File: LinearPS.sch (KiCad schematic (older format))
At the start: 84 parts, among them J1 Conn_01x03, J2 Conn_01x02, J3 Conn_01x03, J4 Conn_01x01, J5 Conn_01x01, J6 Conn_01x01, J7 Conn_01x01, J8 Conn_01x02, Q1 2N2222, Q2 TIP41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

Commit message: Added outputs for voltage and current meters
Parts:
- removed R28, R29: 10k, Resistors_THT:R_Axial_DIN0207_L6.3mm_D2.5mm_P7.62mm_Horizontal, symbol R
- removed U3: LM7805_TO220, TO_SOT_Packages_THT:TO-220-3_Vertical, symbol LM7805_TO220
- added D22: 1N4733A, Diodes_THT:D_DO-41_SOD81_P7.62mm_Horizontal, symbol D_Zener
- added J9: Conn_01x02, Pin_Headers:Pin_Header_Straight_1x02_Pitch2.54mm, symbol Conn_01x02
- added R32: 1k, Resistors_THT:R_Axial_DIN0411_L9.9mm_D3.6mm_P12.70mm_Horizontal, symbol R
- added RV3, RV4, RV5: 10k, Potentiometers:Potentiometer_Trimmer_Bourns_3296W, symbol POT
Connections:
- wire segments 174 -> 184
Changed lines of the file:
@@
-$EndComp
-$Comp
-L R R29
-U 1 1 5CECC88D
-P 10500 5750
-F 0 "R29" V 10580 5750 50  0000 C CNN
-F 1 "10k" V 10500 5750 50  0000 C CNN
-F 2 "Resistors_THT:R_Axial_DIN0207_L6.3mm_D2.5mm_P7.62mm_Horizontal" V 10430 5750 50  0001 C CNN
-F 3 "" H 10500 5750 50  0001 C CNN
-	1    10500 5750
-	0    1    1    0
-$EndComp
-$Comp
-L R R28
-U 1 1 5CECD45F
-P 10150 5650
-F 0 "R28" V 10230 5650 50  0000 C CNN
-F 1 "10k" V 10150 5650 50  0000 C CNN
-F 2 "Resistors_THT:R_Axial_DIN0207_L6.3mm_D2.5mm_P7.62mm_Horizontal" V 10080 5650 50  0001 C CNN
-F 3 "" H 10150 5650 50  0001 C CNN
-	1    10150 5650
-	0    1    1    0
 $EndComp
 $Comp
@@
 $EndComp
 $Comp
-L LM7805_TO220 U3
-U 1 1 5CECF306
-P 2750 2100
-F 0 "U3" H 2600 2225 50  0000 C CNN
-F 1 "LM7805_TO220" H 2750 2225 50  0000 L CNN
-F 2 "TO_SOT_Packages_THT:TO-220-3_Vertical" H 2750 2325 50  0001 C CIN
-F 3 "" H 2750 2050 50  0001 C CNN
-	1    2750 2100
-	1    0    0    -1
-$EndComp
-$Comp
 L GND #PWR2
 U 1 1 5CECFA19
-P 2750 2450
-F 0 "#PWR2" H 2750 2200 50  0001 C CNN
-F 1 "GND" H 2750 2300 50  0000 C CNN
-F 2 "" H 2750 2450 50  0001 C CNN
-F 3 "" H 2750 2450 50  0001 C CNN
-	1    2750 2450
+P 2900 2450
+F 0 "#PWR2" H 2900 2200 50  0001 C CNN
+F 1 "GND" H 2900 2300 50  0000 C CNN
+F 2 "" H 2900 2450 50  0001 C CNN
+F 3 "" H 2900 2450 50  0001 C CNN
+	1    2900 2450
 	1    0    0    -1
 $EndComp
@@
 Connection ~ 5950 3200
 Wire Wire Line
-	5700 3200 5950 3200
+	5700 3200 6050 3200
 Wire Wire Line
 	5950 3000 5050 3000
@@
 	10950 5000 10850 5000
 Wire Wire Line
-	10650 5750 10900 5750
+	10500 5750 10900 5750
 Connection ~ 10950 5000
 Wire Wire Line
@@
 	10850 5300 10850 5000
 Wire Wire Line
-	10300 5650 10900 5650
-Wire Wire Line
-	10000 5700 10000 5650
+	10150 5650 10900 5650
 Wire Wire Line
 	2550 3950 2550 4200
@@
 Connection ~ 2550 3050
 Wire Wire Line
-	2750 2400 2750 2450
-Wire Wire Line
 	3450 2450 3450 2200
 Wire Wire Line
 	3450 2200 3600 2200
 Wire Wire Line
-	3050 2100 3600 2100
+	2800 2100 3600 2100
 Wire Wire Line
 	3150 2450 3150 2450
 Wire Wire Line
-	2300 2100 2450 2100
+	2300 2100 2500 2100
 Wire Wire Line
 	3150 2100 3150 2150
@@
 Wire Wire Line
 	1800 4050 1800 4200
+$Comp
+L R R32
+U 1 1 5CEDBDE6
+P 2650 2100
+F 0 "R32" V 2730 2100 50  0000 C CNN
+F 1 "1k" V 2650 2100 50  0000 C CNN
+F 2 "Resistors_THT:R_Axial_DIN0411_L9.9mm_D3.6mm_P12.70mm_Horizontal" V 2580 2100 50  0001 C CNN
+F 3 "" H 2650 2100 50  0001 C CNN
+	1    2650 2100
+	0    1    1    0
+$EndComp
+$Comp
+L D_Zener D22
+U 1 1 5CEDC7D4
+P 2900 2250
+F 0 "D22" H 2900 2350 50  0000 C CNN
+F 1 "1N4733A" H 2900 2150 50  0000 C CNN
+F 2 "Diodes_THT:D_DO-41_SOD81_P7.62mm_Horizontal" H 2900 2250 50  0001 C CNN
+F 3 "" H 2900 2250 50  0001 C CNN
+	1    2900 2250
+	0    1    1    0
+$EndComp
+Connection ~ 2900 2100
+Wire Wire Line
+	2900 2450 2900 2400
+$Comp
+L POT RV4
+U 1 1 5CEDA0AA
+P 10000 5900
+F 0 "RV4" V 9825 5900 50  0000 C CNN
+F 1 "10k" V 9900 5900 50  0000 C CNN
+F 2 "Potentiometers:Potentiometer_Trimmer_Bourns_3296W" H 10000 5900 50  0001 C CNN
+F 3 "" H 10000 5900 50  0001 C CNN
+	1    10000 5900
+	1    0    0    -1
+$EndComp
+Wire Wire Line
+	10200 5550 10200 6050
+Wire Wire Line
+	10200 6050 10000 6050
+Connection ~ 10200 5550
+Wire Wire Line
+	10150 5900 10150 5650
+Wire Wire Line
+	10000 5700 10000 5750
+$Comp
+L POT RV5
+U 1 1 5CEDAE92
+P 10350 5900
+F 0 "RV5" V 10175 5900 50  0000 C CNN
+F 1 "10k" V 10250 5900 50  0000 C CNN
+F 2 "Potentiometers:Potentiometer_Trimmer_Bourns_3296W" H 10350 5900 50  0001 C CNN
+F 3 "" H 10350 5900 50  0001 C CNN
+	1    10350 5900
+	1    0    0    -1
+$EndComp
+Wire Wire Line
+	10500 5900 10500 5750
+Wire Wire Line
+	10650 5550 10650 6050
+Wire Wire Line
+	10650 6050 10350 6050
+Connection ~ 10650 5550
+$Comp
+L POT RV3
+U 1 1 5CEDB3D7
+P 5600 4500
+F 0 "RV3" V 5425 4500 50  0000 C CNN
+F 1 "10k" V 5500 4500 50  0000 C CNN
+F 2 "Potentiometers:Potentiometer_Trimmer_Bourns_3296W" H 5600 4500 50  0001 C CNN
+F 3 "" H 5600 4500 50  0001 C CNN
+	1    5600 4500
+	-1   0    0    1
+$EndComp
+Wire Wire Line
+	5600 4650 5600 4800
+Connection ~ 5600 4800
+Wire Wire Line
+	5450 4500 5400 4500
+Wire Wire Line
+	5400 4500 5400 4200
+Connection ~ 5400 4200
+$Comp
+L Conn_01x02 J9
+U 1 1 5CEDB976
+P 6250 3200
+F 0 "J9" H 6250 3300 50  0000 C CNN
+F 1 "Conn_01x02" H 6250 3000 50  0000 C CNN
+F 2 "Pin_Headers:Pin_Header_Straight_1x02_Pitch2.54mm" H 6250 3200 50  0001 C CNN
+F 3 "" H 6250 3200 50  0001 C CNN
+	1    6250 3200
+	1    0    0    -1
+$EndComp
+Wire Wire Line
+	6050 3300 6050 4800
+Connection ~ 6050 4800
 $EndSCHEMATC

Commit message: Added better TO-220 mounting
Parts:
- removed D10: 1N4148, Diodes_THT:D_DO-35_SOD27_P7.62mm_Horizontal, symbol D
- removed D7: 1N5339B, Diodes_THT:D_DO-41_SOD81_P7.62mm_Horizontal, symbol D_Zener
- removed J9: Conn_01x02, Pin_Headers:Pin_Header_Straight_1x02_Pitch2.54mm, symbol Conn_01x02
- removed R15: 1k, Resistors_THT:R_Axial_DIN0411_L9.9mm_D3.6mm_P12.70mm_Horizontal, symbol R
- added C13: 100 nF, Capacitors_THT:C_Disc_D5.0mm_W2.5mm_P5.00mm, symbol C
- added D10: 1N4740A, Diodes_THT:D_DO-41_SOD81_P7.62mm_Horizontal, symbol D_Zener
- added D23, D7: 1N4148, Diodes_THT:D_DO-35_SOD27_P7.62mm_Horizontal, symbol D
- added JP1: Jumper_NO_Small, Pin_Headers:Pin_Header_Straight_1x02_Pitch2.54mm, symbol Jumper_NO_Small
- added RV6: 20k, Potentiometers:Potentiometer_Trimmer_Bourns_3296W, symbol POT
- Q2, Q4, Q5, Q6, Q7: footprint TO_SOT_Packages_THT:TO-220-3_Vertical -> linearps:TO-220-3_Vertical_WithPads
- R13: value 56k -> 22k
- R14: value 1k5 -> 1k
- R18: value 56k -> 33k
- RV3: value 10k -> 100k
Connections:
- net GND: now also U2.4 (V-), C13.1, D7.2 (A), JP1.1
- net at C1.1, C10.1, C11.1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: now also D10.1 (K); no longer Q3.1 (E), R19.1, U1.8 (V+)
- net at C4.1, C5.1, C7.2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: now also RV6.1; no longer R11.1, RV3.1
- net at R14.1, R3.1, U1.4 (V-): now also D23.1 (K), JP1.2; no longer U2.4 (V-)
- net at D8.1 (K), R5.2, RV1.1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: now also RV3.2; no longer R18.1
- net at R5.1, R6.1, U1.5 (+): no longer RV3.2
- net at C9.1, Q1.3 (C), U2.1: now also Q2.1 (B)
- net at RV3.3: now also R18.1
- new net: C13.2, D10.2 (A), Q3.1 (E), R19.1, U1.8 (V+)
- new net: R11.1, RV6.2
- new net: D23.2 (A), D7.1 (K)
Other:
- moved on the sheet: C9, R11

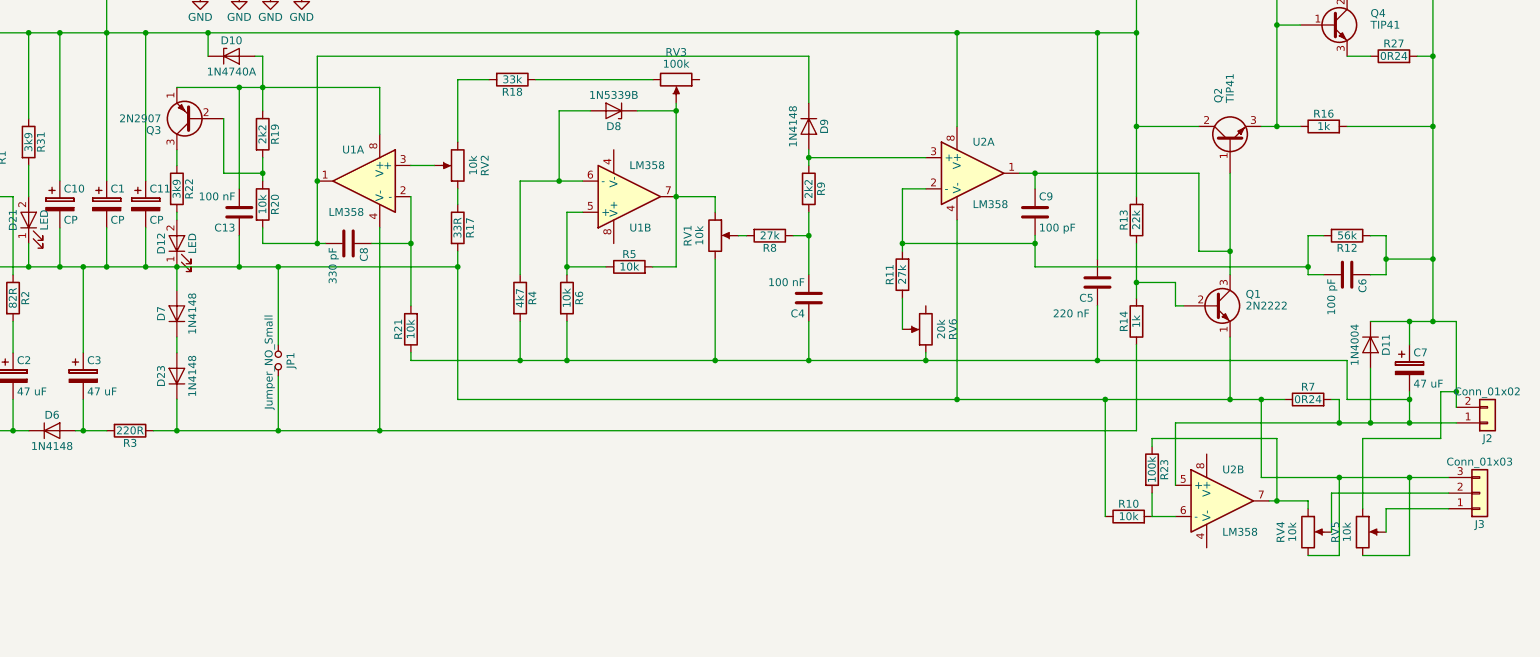
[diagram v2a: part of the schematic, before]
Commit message: Change the voltage and current sense output
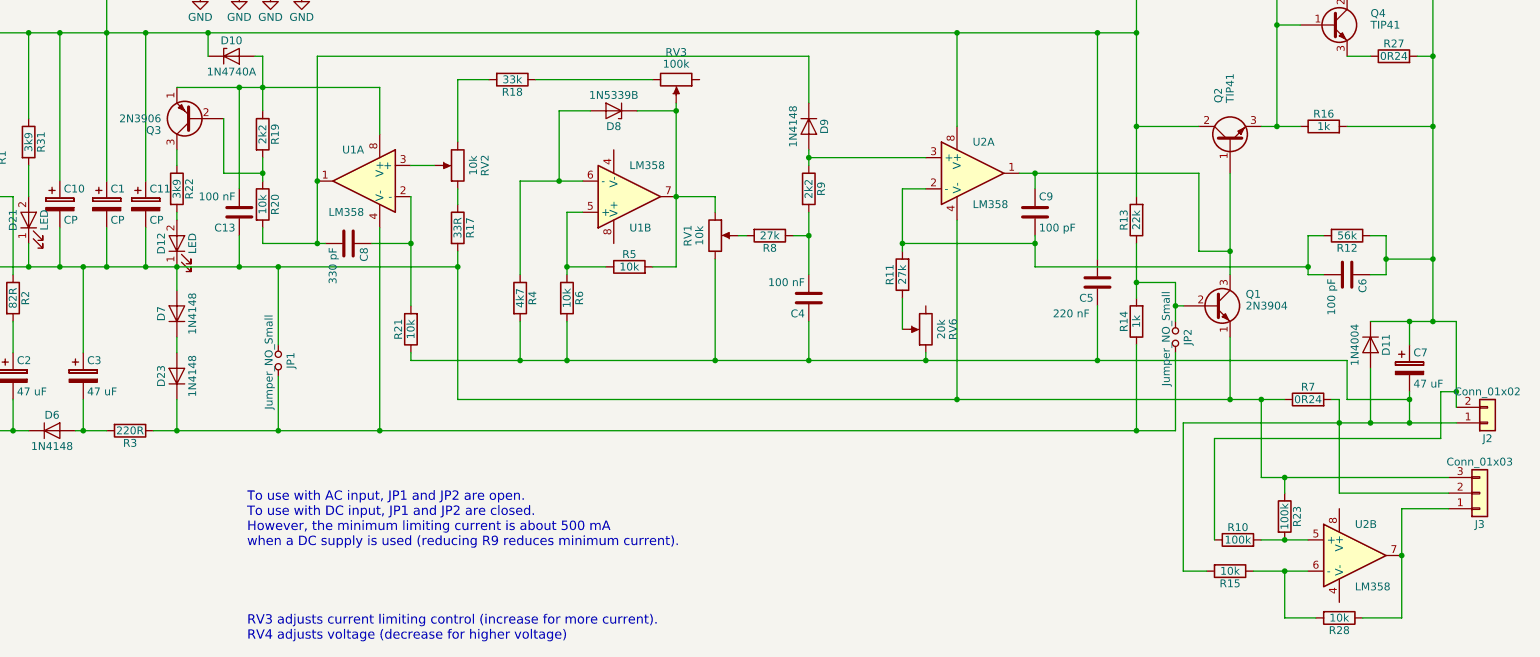
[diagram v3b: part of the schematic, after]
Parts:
- removed RV4, RV5: 10k, Potentiometers:Potentiometer_Trimmer_Bourns_3296W, symbol POT
- added JP2: Jumper_NO_Small, Pin_Headers:Pin_Header_Straight_1x02_Pitch2.54mm, symbol Jumper_NO_Small
- added R15, R28: 10k, Resistors_THT:R_Axial_DIN0207_L6.3mm_D2.5mm_P7.62mm_Horizontal, symbol R
- Q1: value 2N2222 -> 2N3904
- Q3: value 2N2907 -> 2N3906
- R10: value 10k -> 100k
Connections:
- net GND: now also R23.1; no longer R10.1
- net at C4.1, C5.1, C7.2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: now also J3.2 (Pin_2), R15.2; no longer U2.5 (+)
- net at C6.1, C7.1, D11.1 (K)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: now also R10.1
- net at D23.1 (K), JP1.2, R14.1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: now also JP2.2
- net at R10.2, R23.2: now also U2.5 (+); no longer U2.6 (-)
- net at U2.7: now also J3.1 (Pin_1), R28.1; no longer R23.1
- net at Q1.2 (B), R13.1, R14.2: now also JP2.1
- new net: R15.1, R28.2, U2.6 (-)
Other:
- note added: "RV3 adjusts current limiting control (increase for more current).\nRV4 adjusts voltage (decrease for higher voltage)"
- note added: "To use with AC input, JP1 and JP2 are open.\nTo use with DC input, JP1 and JP2 are closed. \nHowever, the minimum limiting current is about 500 mA\nwhen a DC supply is used (reducing R9 reduces minimum current)."
- moved on the sheet: R10, R23, U2B

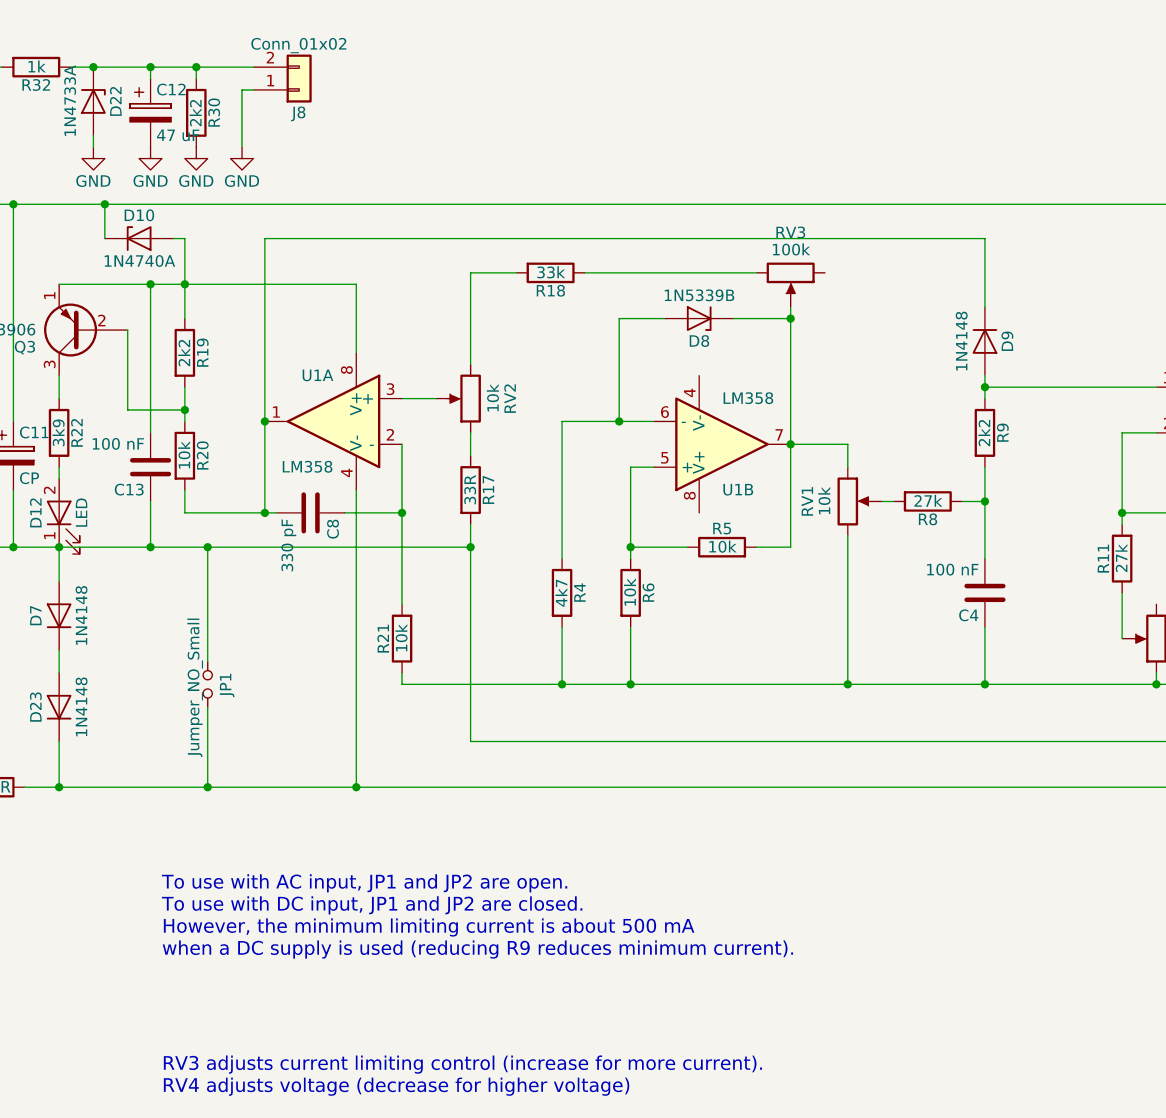
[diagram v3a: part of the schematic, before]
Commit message: Changed voltage and current meter output
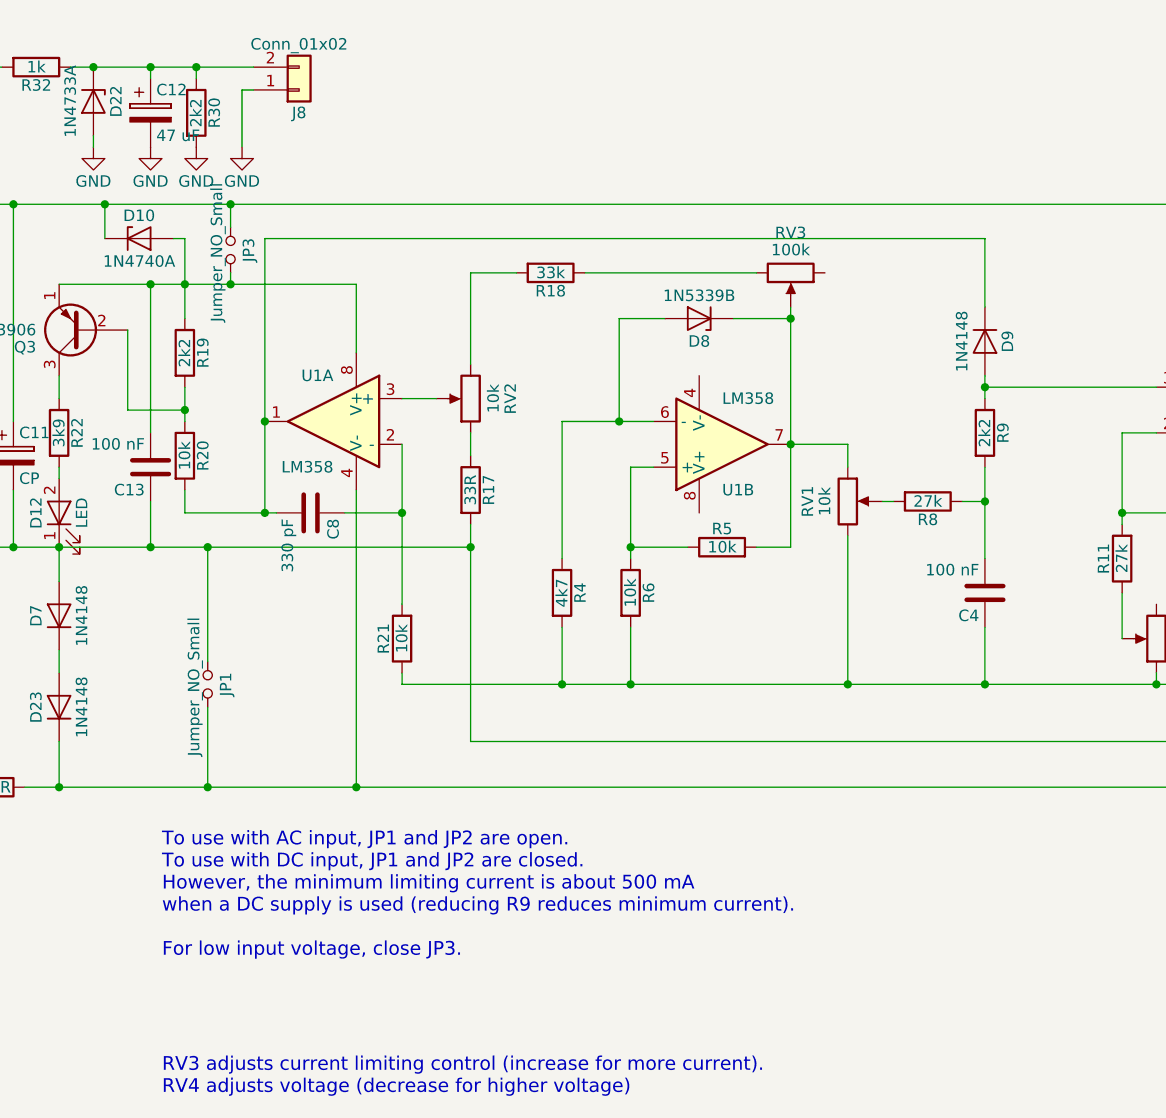
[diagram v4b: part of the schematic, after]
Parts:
- added JP3: Jumper_NO_Small, Pin_Headers:Pin_Header_Straight_1x02_Pitch2.54mm, symbol Jumper_NO_Small
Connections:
- net at C1.1, C10.1, C11.1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: now also JP3.1
- net at C13.2, D10.2 (A), Q3.1 (E)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: now also JP3.2
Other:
- note added: "To use with AC input, JP1 and JP2 are open.\nTo use with DC input, JP1 and JP2 are closed. \nHowever, the minimum limiting current is about 500 mA\nwhen a DC supply is used (reducing R9 reduces minimum current).\n\nFor low input voltage, close JP3."
- note removed: "To use with AC input, JP1 and JP2 are open.\nTo use with DC input, JP1 and JP2 are closed. \nHowever, the minimum limiting current is about 500 mA\nwhen a DC supply is used (reducing R9 reduces minimum current)."
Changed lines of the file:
@@
 $EndComp
 $Comp
-L GND #PWR01
+L GND #PWR1
 U 1 1 5CEC838A
 P 950 4450
-F 0 "#PWR01" H 950 4200 50  0001 C CNN
+F 0 "#PWR1" H 950 4200 50  0001 C CNN
 F 1 "GND" H 950 4300 50  0000 C CNN
 F 2 "" H 950 4450 50  0001 C CNN
@@
 $EndComp
 $Comp
-L GND #PWR02
+L GND #PWR2
 U 1 1 5CECFA19
 P 2900 2450
-F 0 "#PWR02" H 2900 2200 50  0001 C CNN
+F 0 "#PWR2" H 2900 2200 50  0001 C CNN
 F 1 "GND" H 2900 2300 50  0000 C CNN
 F 2 "" H 2900 2450 50  0001 C CNN
@@
 $EndComp
 $Comp
-L GND #PWR03
+L GND #PWR5
 U 1 1 5CED04A2
 P 3550 2450
-F 0 "#PWR03" H 3550 2200 50  0001 C CNN
+F 0 "#PWR5" H 3550 2200 50  0001 C CNN
 F 1 "GND" H 3550 2300 50  0000 C CNN
 F 2 "" H 3550 2450 50  0001 C CNN
@@
 $EndComp
 $Comp
-L GND #PWR04
+L GND #PWR3
 U 1 1 5CED0ACE
 P 3150 2450
-F 0 "#PWR04" H 3150 2200 50  0001 C CNN
+F 0 "#PWR3" H 3150 2200 50  0001 C CNN
 F 1 "GND" H 3150 2300 50  0000 C CNN
 F 2 "" H 3150 2450 50  0001 C CNN
@@
 $EndComp
 $Comp
-L GND #PWR05
+L GND #PWR4
 U 1 1 5CED1C83
 P 3350 2450
-F 0 "#PWR05" H 3350 2200 50  0001 C CNN
+F 0 "#PWR4" H 3350 2200 50  0001 C CNN
 F 1 "GND" H 3350 2300 50  0000 C CNN
 F 2 "" H 3350 2450 50  0001 C CNN
@@
 Connection ~ 9150 4450
 Text Notes 3200 6000 0    60   ~ 0
-To use with AC input, JP1 and JP2 are open.\nTo use with DC input, JP1 and JP2 are closed. \nHowever, the minimum limiting current is about 500 mA\nwhen a DC supply is used (reducing R9 reduces minimum current).
+To use with AC input, JP1 and JP2 are open.\nTo use with DC input, JP1 and JP2 are closed. \nHowever, the minimum limiting current is about 500 mA\nwhen a DC supply is used (reducing R9 reduces minimum current).\n\nFor low input voltage, close JP3.
 Text Notes 3200 6600 0    60   ~ 0
 RV3 adjusts current limiting control (increase for more current).\nRV4 adjusts voltage (decrease for higher voltage)
 Connection ~ 7750 2700
+$Comp
+L Jumper_NO_Small JP3
+U 1 1 5CFE5F75
+P 3500 2900
+F 0 "JP3" H 3500 2980 50  0000 C CNN
+F 1 "Jumper_NO_Small" H 3510 2840 50  0000 C CNN
+F 2 "Pin_Headers:Pin_Header_Straight_1x02_Pitch2.54mm" H 3500 2900 50  0001 C CNN
+F 3 "" H 3500 2900 50  0001 C CNN
+	1    3500 2900
+	0    1    1    0
+$EndComp
+Wire Wire Line
+	3500 2800 3500 2700
+Connection ~ 3500 2700
+Wire Wire Line
+	3500 3000 3500 3050
+Connection ~ 3500 3050
 $EndSCHEMATC
